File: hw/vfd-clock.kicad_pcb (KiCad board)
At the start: 2 copper layers, 139.7 x 49.5 mm, 38 parts, among them CON1 BARREL_JACK_2, CON2 BARREL_JACK_2, P1 ST_LINK, Q1 2N7002P, SW1 SET, SW2 UP, SW3 DOWN, SW4 DIM, U1 Maple_Mini_(BTE14-07), U2 CD4056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

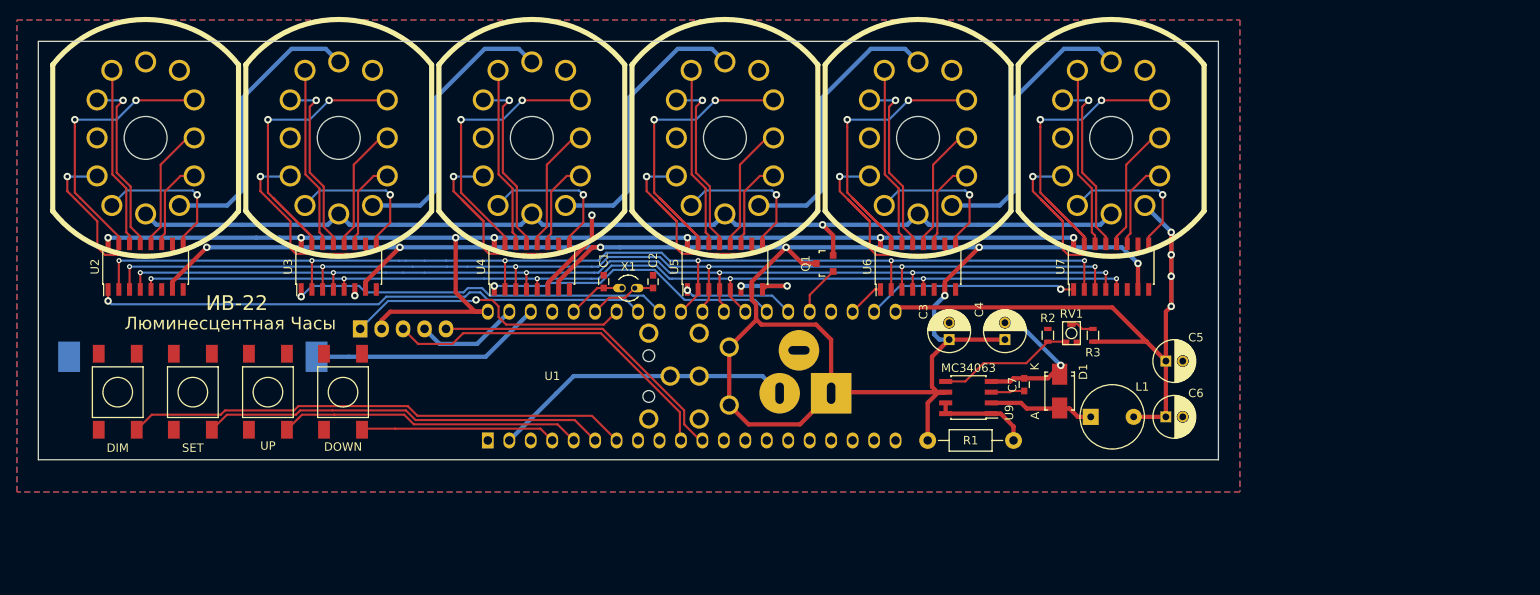
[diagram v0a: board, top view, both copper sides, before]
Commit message: Major hardware rework.
With discrete voltage level shifters, buzzer, pins for a GPS module
addon.
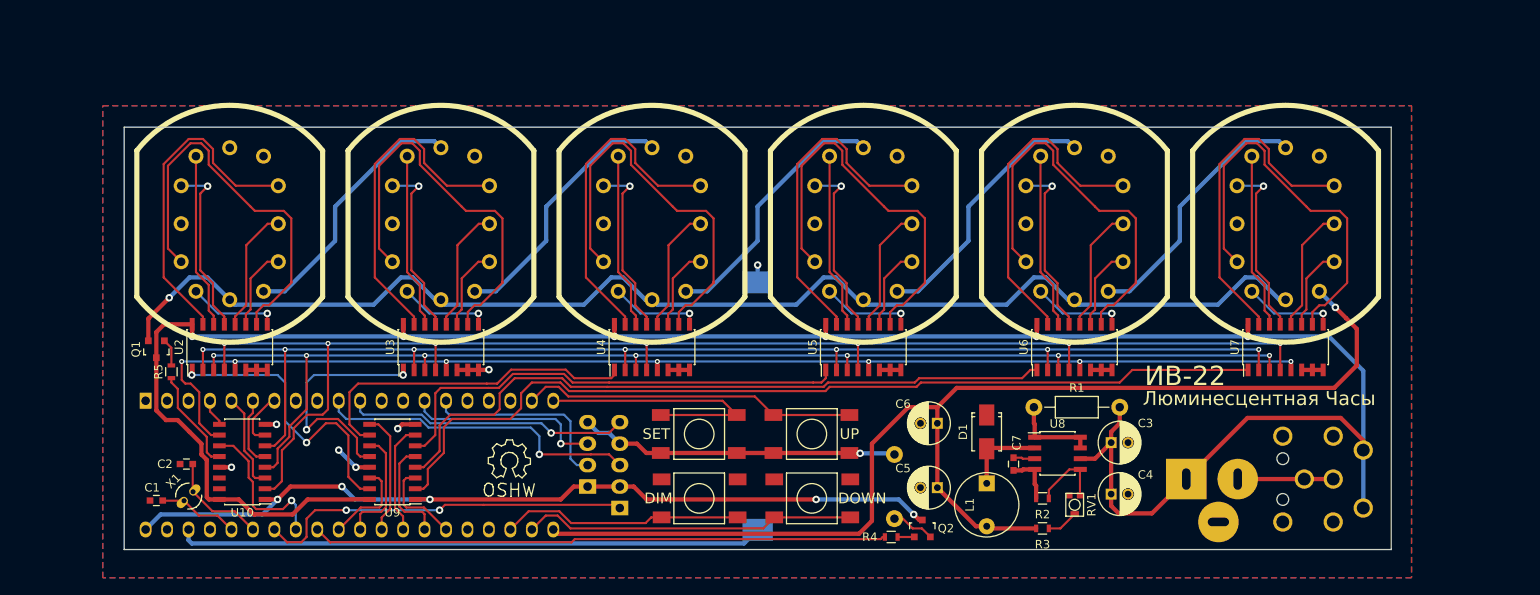
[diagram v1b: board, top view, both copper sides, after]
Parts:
- added P2: GPS, Pin_Headers:Pin_Header_Straight_1x04, B.Cu at (80.3, 67.9)
- added Q2: PNP, VFD:MMBT4403L, F.Cu at (119.9, 72.9)
- added R4: 1k, Resistors_SMD:R_0603, F.Cu at (116.2, 73.9)
- added R5: 1k, Resistors_SMD:R_0603, F.Cu at (31.0, 54.4)
- added SP1: SPEAKER, Buzzers_Beepers:Buzzer_12x9.5RM7.6, B.Cu at (116.6, 67.9)
- added U10: CD4504, Housings_SOIC:SOIC-16_3.9x9.9mm_Pitch1.27mm, F.Cu at (39.4, 65.0)
- added U8: MC34063, Housings_SOIC:SOIC-8_3.9x4.9mm_Pitch1.27mm, F.Cu at (135.9, 64.0)
- P1: footprint Pin_Headers:Pin_Header_Angled_1x05 -> Pin_Headers:Pin_Header_Straight_1x05
- Q1: value 2N7002P -> PNP; footprint Housings_SOT-23_SOT-143_TSOT-6:SOT-23 -> VFD:MMBT4403L
- REF**: moved to F.Cu
- U1: moved to B.Cu
- U9: value MC34063 -> CD4504; footprint Housings_SOIC:SOIC-8_3.9x4.9mm_Pitch1.27mm -> Housings_SOIC:SOIC-16_3.9x9.9mm_Pitch1.27mm
- V1, V2, V3, V4, V5, V6: footprint VFD:DISP_IV-22_SOCKET -> VFD:DISP_IV-22_1PIN_SOCKET
- moved Q1 79.8 mm to (29.2, 51.7), turned to 180 degrees
- moved CON2 76.0 mm to (165.9, 67.1)
- moved REF** 75.4 mm to (71.0, 64.9), turned to 0 degrees
- moved SW4 70.0 mm to (93.5, 69.3), turned to 180 degrees
- moved U9 68.6 mm to (57.1, 65.0)
- moved BT1 67.1 mm to (100.4, 58.4), turned to 270 degrees
- moved SW2 64.6 mm to (106.8, 61.7), turned to 0 degrees
- moved SW1 60.1 mm to (93.5, 61.7), turned to 0 degrees
- moved C2 59.3 mm to (32.8, 65.3), turned to 180 degrees
- moved C1 59.0 mm to (29.2, 69.6), turned to 180 degrees
- moved X1 57.6 mm to (33.0, 69.1), turned to 45 degrees
- moved SW3 56.9 mm to (106.8, 69.3), turned to 180 degrees
- moved CON1 55.2 mm to (157.2, 67.1), turned to 180 degrees
- moved U1 41.9 mm to (52.1, 65.4)
- moved P1 37.3 mm to (84.1, 70.5), turned to 0 degrees
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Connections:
- Q1 pad 1: /GRID_PWM -> /GRID
- Q1 pad 2: /GRID -> Net-(Q1-Pad2)
- U1 pad 14: (no net) -> /GPS_TX
- U1 pad 15: (no net) -> /GPS_RX
- U1 pad 19: (no net) -> /BTN_UP
- U1 pad 20: (no net) -> /BTN_SET
- U1 pad 22: /STROBE6 -> /BTN_DN
- U1 pad 23: /STROBE5 -> /BTN_DIM
- U1 pad 25: /GRID_PWM -> (no net)
- U1 pad 26: /STROBE4 -> /STROBE6L
- U1 pad 27: /STROBE3 -> /STROBE5L
- U1 pad 28: /DA -> /STROBE4L
- U1 pad 29: /DD -> /STROBE3L
- U1 pad 30: /DB -> /STROBE2L
- U1 pad 31: /DC -> /STROBE1L
- U1 pad 32: /STROBE2 -> /BUZ
- U1 pad 33: /STROBE1 -> /GRIDL
- U1 pad 4: /BTN_DN -> /DAL
- U1 pad 5: /BTN_UP -> /DDL
- U1 pad 6: /BTN_SET -> /DBL
- U1 pad 7: /BTN_DIM -> /DCL
- U2 pad 1: /STROBE1 -> /STROBE1H
- U2 pad 16: /3v3 -> /19v5
- U2 pad 2: /DC -> /DCH
- U2 pad 3: /DB -> /DBH
- U2 pad 4: /DD -> /DDH
- U2 pad 5: /DA -> /DAH
- U2 pad 7: /19v5 -> /GND
- U3 pad 1: /STROBE2 -> /STROBE2H
- U3 pad 16: /3v3 -> /19v5
- U3 pad 2: /DC -> /DCH
- U3 pad 3: /DB -> /DBH
- U3 pad 4: /DD -> /DDH
- U3 pad 5: /DA -> /DAH
- U3 pad 7: /19v5 -> /GND
- U4 pad 1: /STROBE3 -> /STROBE3H
- U4 pad 16: /3v3 -> /19v5
- U4 pad 2: /DC -> /DCH
- U4 pad 3: /DB -> /DBH
- U4 pad 4: /DD -> /DDH
- U4 pad 5: /DA -> /DAH
- U4 pad 7: /19v5 -> /GND
- U5 pad 1: /STROBE4 -> /STROBE4H
- U5 pad 16: /3v3 -> /19v5
- U5 pad 2: /DC -> /DCH
- U5 pad 3: /DB -> /DBH
- U5 pad 4: /DD -> /DDH
- U5 pad 5: /DA -> /DAH
- U5 pad 7: /19v5 -> /GND
- U6 pad 1: /STROBE5 -> /STROBE5H
- U6 pad 16: /3v3 -> /19v5
- U6 pad 2: /DC -> /DCH
- U6 pad 3: /DB -> /DBH
- U6 pad 4: /DD -> /DDH
- U6 pad 5: /DA -> /DAH
- U6 pad 7: /19v5 -> /GND
- U7 pad 1: /STROBE6 -> /STROBE6H
- U7 pad 16: /3v3 -> /19v5
- U7 pad 2: /DC -> /DCH
- U7 pad 3: /DB -> /DBH
- U7 pad 4: /DD -> /DDH
- U7 pad 5: /DA -> /DAH
- U7 pad 7: /19v5 -> /GND
- U9 pad 1: /REG_HI -> /3v3
- U9 pad 2: Net-(D1-Pad2) -> /STROBE6H
- U9 pad 3: Net-(C7-Pad2) -> /STROBE6L
- U9 pad 4: /GND -> /STROBE5H
- U9 pad 5: Net-(R2-Pad1) -> /STROBE5L
- U9 pad 6: /19v5 -> /STROBE4H
- U9 pad 7: /REG_HI -> /STROBE4L
- U9 pad 8: /REG_HI -> /GND
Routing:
- net /DDH: track 0.00 -> 165.8 mm, vias 0 -> 7
- net /DCH: track 0.00 -> 152.9 mm, vias 0 -> 7
- net /DBH: track 0.00 -> 151.1 mm, vias 0 -> 7
- net /DAH: track 0.00 -> 148.8 mm, vias 0 -> 7
- net /DC: track 139.0 -> 0.00 mm, vias 6 -> 0
- net /DB: track 134.4 -> 0.00 mm, vias 6 -> 0
- net /DD: track 130.2 -> 0.00 mm, vias 6 -> 0
- net /DA: track 126.9 -> 0.00 mm, vias 6 -> 0
- net /STROBE6H: track 0.00 -> 109.2 mm
- net /STROBE5H: track 0.00 -> 82.1 mm
- net /BUZ: track 0.00 -> 68.1 mm
- net /STROBE1: track 65.8 -> 0.00 mm, vias 1 -> 0
- net /7v2: track 80.6 -> 142.8 mm, vias 4 -> 1
- net /STROBE4H: track 0.00 -> 56.6 mm
- net /STROBE2: track 45.5 -> 0.00 mm, vias 1 -> 0
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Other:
- board size 139.7 x 49.5 mm -> 150 x 50 mm
- board text added: "SWDIO GND SWCLK 3v3 RST"
- board text removed: "RST 3v3 CLK GND DIO"

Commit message: various small tweaks
including switch the VFD tube outline from silkscreen to fab layer
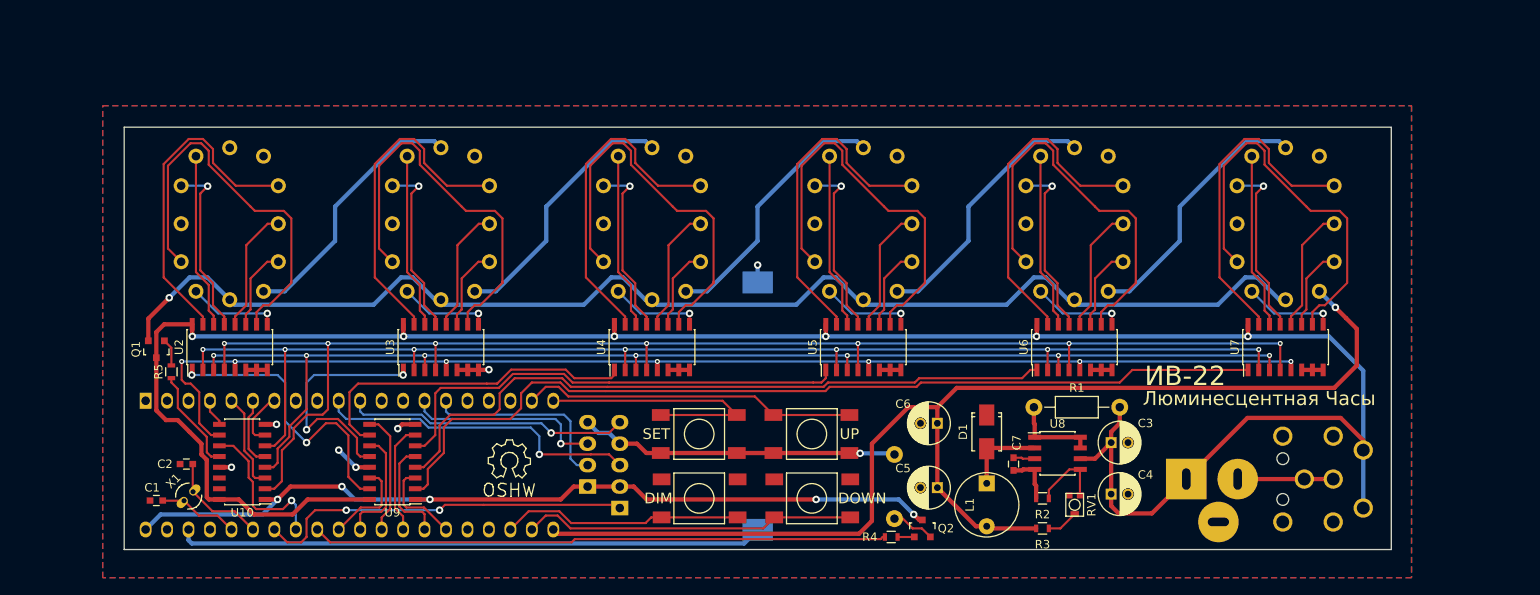
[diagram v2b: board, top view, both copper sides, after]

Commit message: Fix VFD pinout.
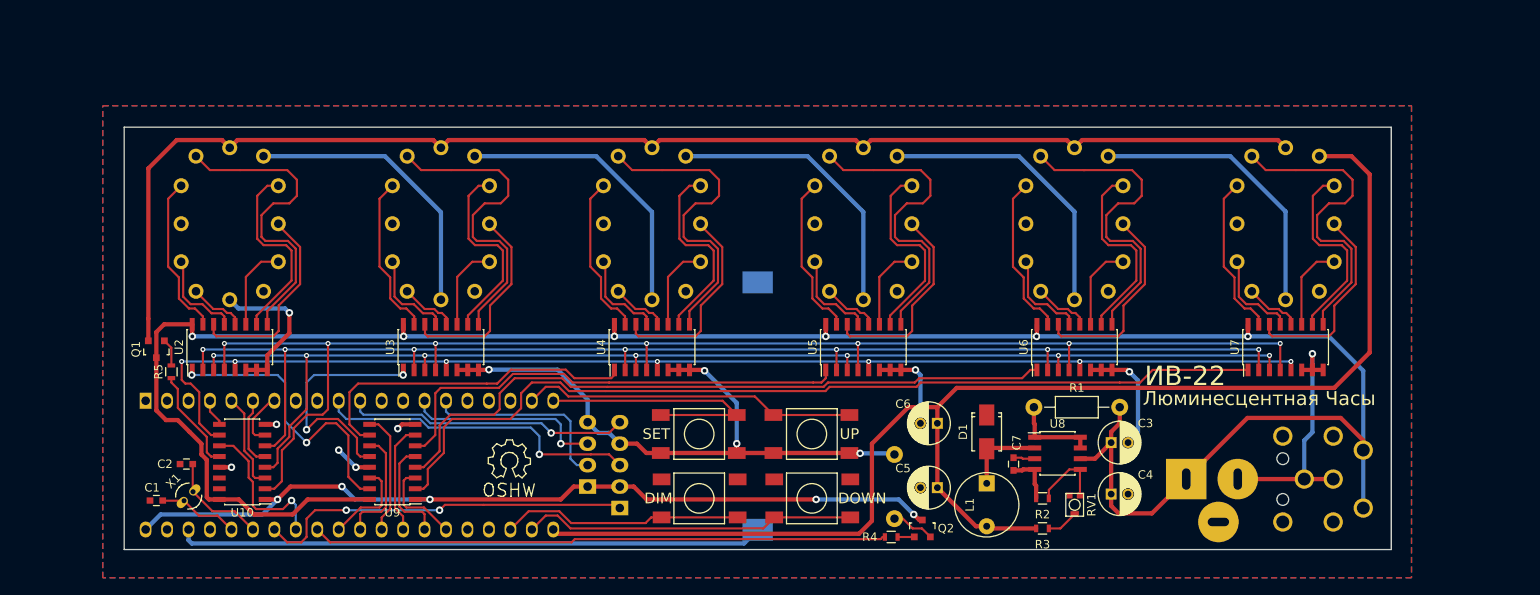
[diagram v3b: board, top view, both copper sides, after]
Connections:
- net Net-(U2-Pad11) renamed /C1
- net Net-(U3-Pad11) renamed /C2
- net Net-(U4-Pad11) renamed /C3
- net Net-(U5-Pad11) renamed /C4
- net Net-(U6-Pad11) renamed /C5
- net Net-(U7-Pad11) renamed /C6
- U2 pad 10: Net-(U2-Pad10) -> /B1
- U2 pad 12: Net-(U2-Pad12) -> /D1
- U2 pad 13: Net-(U2-Pad13) -> /E1
- U2 pad 14: Net-(U2-Pad14) -> /G1
- U2 pad 15: Net-(U2-Pad15) -> /F1
- U2 pad 9: Net-(U2-Pad9) -> /A1
- U3 pad 10: Net-(U3-Pad10) -> /B2
- U3 pad 12: Net-(U3-Pad12) -> /D2
- U3 pad 13: Net-(U3-Pad13) -> /E2
- U3 pad 14: Net-(U3-Pad14) -> /G2
- U3 pad 15: Net-(U3-Pad15) -> /F2
- U3 pad 9: Net-(U3-Pad9) -> /A2
- U4 pad 10: Net-(U4-Pad10) -> /B3
- U4 pad 12: Net-(U4-Pad12) -> /D3
- U4 pad 13: Net-(U4-Pad13) -> /E3
- U4 pad 14: Net-(U4-Pad14) -> /G3
- U4 pad 15: Net-(U4-Pad15) -> /F3
- U4 pad 9: Net-(U4-Pad9) -> /A3
- U5 pad 10: Net-(U5-Pad10) -> /B4
- U5 pad 12: Net-(U5-Pad12) -> /D4
- U5 pad 13: Net-(U5-Pad13) -> /E4
- U5 pad 14: Net-(U5-Pad14) -> /G4
- U5 pad 15: Net-(U5-Pad15) -> /F4
- U5 pad 9: Net-(U5-Pad9) -> /A4
- U6 pad 10: Net-(U6-Pad10) -> /B5
- U6 pad 12: Net-(U6-Pad12) -> /D5
- U6 pad 13: Net-(U6-Pad13) -> /E5
- U6 pad 14: Net-(U6-Pad14) -> /G5
- U6 pad 15: Net-(U6-Pad15) -> /F5
- U6 pad 9: Net-(U6-Pad9) -> /A5
- U7 pad 10: Net-(U7-Pad10) -> /B6
- U7 pad 12: Net-(U7-Pad12) -> /D6
- U7 pad 13: Net-(U7-Pad13) -> /E6
- U7 pad 14: Net-(U7-Pad14) -> /G6
- U7 pad 15: Net-(U7-Pad15) -> /F6
- U7 pad 9: Net-(U7-Pad9) -> /A6
- V1 pad 1: (no net) -> /FIL1
- V1 pad 10: Net-(U2-Pad13) -> /F1
- V1 pad 11: Net-(U2-Pad14) -> /A1
- V1 pad 12: /GND -> /GRID
- V1 pad 2: Net-(U2-Pad15) -> /B1
- V1 pad 3: Net-(U2-Pad12) -> /G1
- V1 pad 5: /FIL1 -> (no net)
- V1 pad 6: /GRID -> /GND
- V1 pad 7: Net-(U2-Pad9) -> /D1
- V1 pad 8: Net-(U2-Pad10) -> /E1
- V2 pad 1: (no net) -> /FIL2
- V2 pad 10: Net-(U3-Pad13) -> /F2
- V2 pad 11: Net-(U3-Pad14) -> /A2
- V2 pad 12: /FIL1 -> /GRID
- V2 pad 2: Net-(U3-Pad15) -> /B2
- V2 pad 3: Net-(U3-Pad12) -> /G2
- V2 pad 5: /FIL2 -> (no net)
- V2 pad 6: /GRID -> /FIL1
- V2 pad 7: Net-(U3-Pad9) -> /D2
- V2 pad 8: Net-(U3-Pad10) -> /E2
- V3 pad 1: (no net) -> /FIL3
- V3 pad 10: Net-(U4-Pad13) -> /F3
- V3 pad 11: Net-(U4-Pad14) -> /A3
- V3 pad 12: /FIL2 -> /GRID
- V3 pad 2: Net-(U4-Pad15) -> /B3
- V3 pad 3: Net-(U4-Pad12) -> /G3
- V3 pad 5: /FIL3 -> (no net)
- V3 pad 6: /GRID -> /FIL2
- V3 pad 7: Net-(U4-Pad9) -> /D3
- V3 pad 8: Net-(U4-Pad10) -> /E3
- V4 pad 1: (no net) -> /FIL4
- V4 pad 10: Net-(U5-Pad13) -> /F4
- V4 pad 11: Net-(U5-Pad14) -> /A4
- V4 pad 12: /FIL3 -> /GRID
- V4 pad 2: Net-(U5-Pad15) -> /B4
- V4 pad 3: Net-(U5-Pad12) -> /G4
- V4 pad 5: /FIL4 -> (no net)
- V4 pad 6: /GRID -> /FIL3
- V4 pad 7: Net-(U5-Pad9) -> /D4
- V4 pad 8: Net-(U5-Pad10) -> /E4
- V5 pad 1: (no net) -> /FIL5
- V5 pad 10: Net-(U6-Pad13) -> /F5
- V5 pad 11: Net-(U6-Pad14) -> /A5
- V5 pad 12: /FIL4 -> /GRID
- V5 pad 2: Net-(U6-Pad15) -> /B5
- V5 pad 3: Net-(U6-Pad12) -> /G5
- V5 pad 5: /FIL5 -> (no net)
- V5 pad 6: /GRID -> /FIL4
- V5 pad 7: Net-(U6-Pad9) -> /D5
- V5 pad 8: Net-(U6-Pad10) -> /E5
- V6 pad 1: (no net) -> /7v2
- V6 pad 10: Net-(U7-Pad13) -> /F6
- V6 pad 11: Net-(U7-Pad14) -> /A6
- V6 pad 12: /FIL5 -> /GRID
- V6 pad 2: Net-(U7-Pad15) -> /B6
- V6 pad 3: Net-(U7-Pad12) -> /G6
- V6 pad 5: /7v2 -> (no net)
- V6 pad 6: /GRID -> /FIL5
- V6 pad 7: Net-(U7-Pad9) -> /D6
- V6 pad 8: Net-(U7-Pad10) -> /E6
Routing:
- net /GND: track 84.1 -> 163.5 mm, vias 8 -> 13
- net Net-(U7-Pad10): track 47.0 -> 0.00 mm
- net Net-(U4-Pad10): track 47.0 -> 0.00 mm
- net Net-(U3-Pad10): track 47.0 -> 0.00 mm
- net Net-(U2-Pad10): track 47.0 -> 0.00 mm
- net Net-(U5-Pad10): track 47.0 -> 0.00 mm
- net Net-(U6-Pad10): track 47.0 -> 0.00 mm
- net Net-(U5-Pad15): track 39.0 -> 0.00 mm
- net Net-(U3-Pad15): track 39.0 -> 0.00 mm
- net Net-(U2-Pad15): track 39.0 -> 0.00 mm
- net Net-(U6-Pad15): track 39.0 -> 0.00 mm
- net Net-(U4-Pad15): track 39.0 -> 0.00 mm
- net Net-(U7-Pad15): track 39.0 -> 0.00 mm
- net /A5: track 0.00 -> 37.9 mm
- net /A2: track 0.00 -> 37.7 mm
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
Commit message: VFD trace tweak, label font size
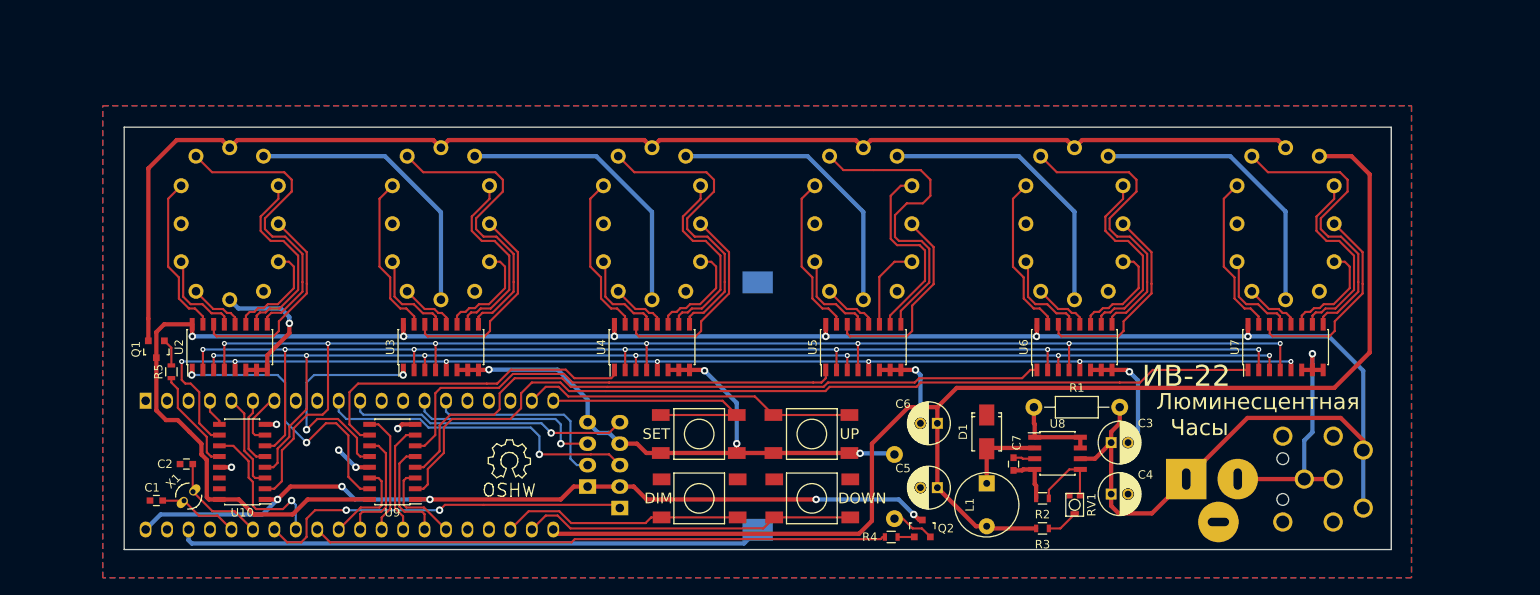
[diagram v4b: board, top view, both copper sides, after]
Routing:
- net /C6: track 10.2 -> 12.7 mm
- net /C3: track 10.2 -> 12.7 mm
- net /C2: track 10.2 -> 12.7 mm
- net /C1: track 10.2 -> 12.7 mm
- net /C5: track 10.2 -> 12.7 mm
- net /A5: track 37.9 -> 36.1 mm
- net /A2: track 37.7 -> 36.1 mm
- net /A1: track 37.7 -> 36.1 mm
- net /A3: track 37.7 -> 36.1 mm
- net /A6: track 37.7 -> 36.1 mm
- net /G6: track 24.0 -> 24.8 mm
- net /G5: track 24.0 -> 24.8 mm
- net /G1: track 24.0 -> 24.8 mm
- net /G3: track 24.0 -> 24.8 mm
- net /G2: track 24.0 -> 24.7 mm
